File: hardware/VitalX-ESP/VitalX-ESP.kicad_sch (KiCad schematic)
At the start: 56 parts, among them J1 EGC Probe, J2 GSR Probe, J3 UART, J4 JTAG, J5 Power terminal, Q1 BSS138, SW2 Reset, U1 AD8232ACPZ-R7, U3 ADP160AUJZ-1.8-R7, U4 ADPD144RI-ACEZ-RL, U5 AMS1117-3.3, U6 MCP601-xOT, U7 ESP32-S2-WROOM

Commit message: [nightly] Change naming convertion.
+3.3V -> +3V3.
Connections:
- net +3.3V is gone; now on net +3V3: C5.2, R13.2, R15.2, R3.2, R4.2, U1.15 (FR), U1.17 (VS+)
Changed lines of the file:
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@@
     (rev "Sample A")
   )
-  (junction (at 135.255 224.155) (diameter 0) (color 0 0 0 0)
-  )
   (junction (at 99.695 66.675) (diameter 0) (color 0 0 0 0)
   )
@@
   (junction (at 74.295 203.835) (diameter 0) (color 0 0 0 0)
   )
+  (junction (at 135.255 224.155) (diameter 0) (color 0 0 0 0)
+  )
   (junction (at 88.265 227.965) (diameter 0) (color 0 0 0 0)
   )
@@
     )
   )
+  (symbol (lib_id "power:+3V3") (at 184.15 103.505 0) (unit 1)
+    (in_bom yes) (on_board yes) (dnp no) (fields_autoplaced)
+    (property "Reference" "#PWR09" (at 184.15 107.315 0)
+      (effects (font (size 1.27 1.27)) hide)
+    )
+    (property "Value" "+3V3" (at 184.15 99.06 0)
+      (effects (font (size 1.27 1.27)))
+    )
+    (property "Footprint" "" (at 184.15 103.505 0)
+      (effects (font (size 1.27 1.27)) hide)
+    )
+    (property "Datasheet" "" (at 184.15 103.505 0)
+      (effects (font (size 1.27 1.27)) hide)
+    )
+    (pin "1")
+    (instances
+      (project "VitalX-ESP"
+        (path "/c6ad7dc7-b487-4ed9-a043-5d3a4b3b13ea"
+          (reference "#PWR09") (unit 1)
+        )
+      )
+    )
+  )
   (symbol (lib_id "Switch:SW_Push") (at 88.9 109.855 0) (unit 1)
     (in_bom yes) (on_board yes) (dnp no) (fields_autoplaced)
@@
     )
   )
+  (symbol (lib_id "power:+3V3") (at 74.295 201.295 0) (unit 1)
+    (in_bom yes) (on_board yes) (dnp no) (fields_autoplaced)
+    (property "Reference" "#PWR06" (at 74.295 205.105 0)
+      (effects (font (size 1.27 1.27)) hide)
+    )
+    (property "Value" "+3V3" (at 74.295 196.85 0)
+      (effects (font (size 1.27 1.27)))
+    )
+    (property "Footprint" "" (at 74.295 201.295 0)
+      (effects (font (size 1.27 1.27)) hide)
+    )
+    (property "Datasheet" "" (at 74.295 201.295 0)
+      (effects (font (size 1.27 1.27)) hide)
+    )
+    (pin "1")
+    (instances
+      (project "VitalX-ESP"
+        (path "/c6ad7dc7-b487-4ed9-a043-5d3a4b3b13ea"
+          (reference "#PWR06") (unit 1)
+        )
+      )
+    )
+  )
   (symbol (lib_id "Device:R") (at 143.51 213.995 90) (unit 1)
     (in_bom yes) (on_board yes) (dnp no)
@@
     )
   )
+  (symbol (lib_id "power:+3V3") (at 135.255 224.155 0) (unit 1)
+    (in_bom yes) (on_board yes) (dnp no) (fields_autoplaced)
+    (property "Reference" "#PWR07" (at 135.255 227.965 0)
+      (effects (font (size 1.27 1.27)) hide)
+    )
+    (property "Value" "+3V3" (at 135.255 219.71 0)
+      (effects (font (size 1.27 1.27)))
+    )
+    (property "Footprint" "" (at 135.255 224.155 0)
+      (effects (font (size 1.27 1.27)) hide)
+    )
+    (property "Datasheet" "" (at 135.255 224.155 0)
+      (effects (font (size 1.27 1.27)) hide)
+    )
+    (pin "1")
+    (instances
+      (project "VitalX-ESP"
+        (path "/c6ad7dc7-b487-4ed9-a043-5d3a4b3b13ea"
+          (reference "#PWR07") (unit 1)
+        )
+      )
+    )
+  )
   (symbol (lib_id "Device:C_Small") (at 114.935 206.375 90) (unit 1)
     (in_bom yes) (on_board yes) (dnp no)
@@
     )
   )
+  (symbol (lib_id "power:+3V3") (at 107.315 183.515 0) (unit 1)
+    (in_bom yes) (on_board yes) (dnp no) (fields_autoplaced)
+    (property "Reference" "#PWR052" (at 107.315 187.325 0)
+      (effects (font (size 1.27 1.27)) hide)
+    )
+    (property "Value" "+3V3" (at 107.315 179.07 0)
+      (effects (font (size 1.27 1.27)))
+    )
+    (property "Footprint" "" (at 107.315 183.515 0)
+      (effects (font (size 1.27 1.27)) hide)
+    )
+    (property "Datasheet" "" (at 107.315 183.515 0)
+      (effects (font (size 1.27 1.27)) hide)
+    )
+    (pin "1")
+    (instances
+      (project "VitalX-ESP"
+        (path "/c6ad7dc7-b487-4ed9-a043-5d3a4b3b13ea"
+          (reference "#PWR052") (unit 1)
+        )
+      )
+    )
+  )
   (symbol (lib_id "Device:R") (at 81.915 210.185 180) (unit 1)
     (in_bom yes) (on_board yes) (dnp no)
@@
     )
   )
-  (symbol (lib_id "power:+3.3V") (at 184.15 103.505 0) (unit 1)
-    (in_bom yes) (on_board yes) (dnp no)
-    (property "Reference" "#PWR012" (at 184.15 107.315 0)
-      (effects (font (size 1.27 1.27)) hide)
-    )
-    (property "Value" "+3.3V" (at 181.61 99.695 0)
-      (effects (font (size 1.27 1.27)) (justify left))
-    )
-    (property "Footprint" "" (at 184.15 103.505 0)
-      (effects (font (size 1.27 1.27)) hide)
-    )
-    (property "Datasheet" "" (at 184.15 103.505 0)
-      (effects (font (size 1.27 1.27)) hide)
-    )
-    (pin "1")
-    (instances
-      (project "VitalX-ESP"
-        (path "/c6ad7dc7-b487-4ed9-a043-5d3a4b3b13ea"
-          (reference "#PWR012") (unit 1)
-        )
-      )
-    )
-  )
   (symbol (lib_id "power:GND") (at 145.415 233.045 90) (unit 1)
     (in_bom yes) (on_board yes) (dnp no)
@@
     )
   )
-  (symbol (lib_id "power:+3.3V") (at 145.415 230.505 270) (unit 1)
-    (in_bom yes) (on_board yes) (dnp no)
-    (property "Reference" "#PWR04" (at 141.605 230.505 0)
-      (effects (font (size 1.27 1.27)) hide)
-    )
-    (property "Value" "+3.3V" (at 147.955 230.505 90)
-      (effects (font (size 1.27 1.27)) (justify left))
-    )
-    (property "Footprint" "" (at 145.415 230.505 0)
-      (effects (font (size 1.27 1.27)) hide)
-    )
-    (property "Datasheet" "" (at 145.415 230.505 0)
-      (effects (font (size 1.27 1.27)) hide)
-    )
-    (pin "1")
-    (instances
-      (project "VitalX-ESP"
-        (path "/c6ad7dc7-b487-4ed9-a043-5d3a4b3b13ea"
-          (reference "#PWR04") (unit 1)
-        )
-      )
-    )
-  )
   (symbol (lib_id "power:GND") (at 320.04 61.595 0) (unit 1)
     (in_bom yes) (on_board yes) (dnp no) (fields_autoplaced)
@@
     )
   )
+  (symbol (lib_id "power:+3V3") (at 145.415 230.505 270) (unit 1)
+    (in_bom yes) (on_board yes) (dnp no) (fields_autoplaced)
+    (property "Reference" "#PWR04" (at 141.605 230.505 0)
+      (effects (font (size 1.27 1.27)) hide)
+    )
+    (property "Value" "+3V3" (at 148.59 230.505 90)
+      (effects (font (size 1.27 1.27)) (justify left))
+    )
+    (property "Footprint" "" (at 145.415 230.505 0)
+      (effects (font (size 1.27 1.27)) hide)
+    )
+    (property "Datasheet" "" (at 145.415 230.505 0)
+      (effects (font (size 1.27 1.27)) hide)
+    )
+    (pin "1")
+    (instances
+      (project "VitalX-ESP"
+        (path "/c6ad7dc7-b487-4ed9-a043-5d3a4b3b13ea"
+          (reference "#PWR04") (unit 1)
+        )
+      )
+    )
+  )
   (symbol (lib_id "Device:R") (at 92.075 250.825 180) (unit 1)
     (in_bom yes) (on_board yes) (dnp no)
@@
     )
   )
-  (symbol (lib_id "power:+3.3V") (at 135.255 224.155 0) (unit 1)
-    (in_bom yes) (on_board yes) (dnp no)
-    (property "Reference" "#PWR07" (at 135.255 227.965 0)
-      (effects (font (size 1.27 1.27)) hide)
-    )
-    (property "Value" "+3.3V" (at 132.08 220.345 0)
-      (effects (font (size 1.27 1.27)) (justify left))
-    )
-    (property "Footprint" "" (at 135.255 224.155 0)
-      (effects (font (size 1.27 1.27)) hide)
-    )
-    (property "Datasheet" "" (at 135.255 224.155 0)
-      (effects (font (size 1.27 1.27)) hide)
-    )
-    (pin "1")
-    (instances
-      (project "VitalX-ESP"
-        (path "/c6ad7dc7-b487-4ed9-a043-5d3a4b3b13ea"
-          (reference "#PWR07") (unit 1)
-        )
-      )
-    )
-  )
   (symbol (lib_id "AD8232ACPZ:AD8232ACPZ-R7") (at 95.885 213.995 0) (unit 1)
     (in_bom yes) (on_board yes) (dnp no)
@@
     )
   )
-  (symbol (lib_id "power:+3.3V") (at 74.295 201.295 0) (unit 1)
-    (in_bom yes) (on_board yes) (dnp no)
-    (property "Reference" "#PWR06" (at 74.295 205.105 0)
-      (effects (font (size 1.27 1.27)) hide)
-    )
-    (property "Value" "+3.3V" (at 74.295 197.485 0)
-      (effects (font (size 1.27 1.27)))
-    )
-    (property "Footprint" "" (at 74.295 201.295 0)
-      (effects (font (size 1.27 1.27)) hide)
-    )
-    (property "Datasheet" "" (at 74.295 201.295 0)
-      (effects (font (size 1.27 1.27)) hide)
-    )
-    (pin "1")
-    (instances
-      (project "VitalX-ESP"
-        (path "/c6ad7dc7-b487-4ed9-a043-5d3a4b3b13ea"
-          (reference "#PWR06") (unit 1)
-        )
-      )
-    )
-  )
   (symbol (lib_id "power:GND") (at 107.315 188.595 0) (unit 1)
     (in_bom yes) (on_board yes) (dnp no) (fields_autoplaced)
@@
         )
       )
-    )
-  )
-  (symbol (lib_id "power:+3.3V") (at 107.315 183.515 0) (unit 1)
-    (in_bom yes) (on_board yes) (dnp no)
-    (property "Reference" "#PWR09" (at 107.315 187.325 0)
-      (effects (font (size 1.27 1.27)) hide)
-    )
-    (property "Value" "+3.3V" (at 107.315 179.705 0)
-      (effects (font (size 1.27 1.27)))
-    )
-    (property "Footprint" "" (at 107.315 183.515 0)
-      (effects (font (size 1.27 1.27)) hide)
-    )
-    (property "Datasheet" "" (at 107.315 183.515 0)
-      (effects (font (size 1.27 1.27)) hide)
-    )
-    (pin "1")
-    (instances
-      (project "VitalX-ESP"
-        (path "/c6ad7dc7-b487-4ed9-a043-5d3a4b3b13ea"
-          (reference "#PWR09") (unit 1)
-        )
-      )

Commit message: [nightly] Change ECG Probe footprint.
Changes in accordance with reference design.
- https://www.snapeda.com/parts/SJ2-3593D-SMT-TR/CUI%20Devices/view-part/?ref=mouser
- https://easyeda.com/editor#project_id=8294b8a1d6874413ae900972098163d6
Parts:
- removed J1: EGC Probe, Connector_Audio:Jack_3.5mm_KoreanHropartsElec_PJ-320D-4A_Horizontal, symbol Connector_Audio:AudioJack4
- added J1: ECG Probe, AUDIO_SJ2-3593D-SMT-TR:SJ2-3593D-SMT-TR, symbol Connector_Audio:AudioJack3
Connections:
- net LA: now also J1.R
- net RA: now also J1.T
- net RL: now also J1.S
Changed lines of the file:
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@@
     (stroke (width 0) (type default))
   )
-  (wire (pts (xy 45.085 194.31) (xy 53.975 194.31))
-    (stroke (width 0) (type default))
-  )
   (wire (pts (xy 353.695 194.31) (xy 353.695 198.12))
     (stroke (width 0) (type default))
@@
     (effects (font (size 1.27 1.27)) (justify left bottom))
   )
-  (label "RA" (at 53.975 196.85 180) (fields_autoplaced)
+  (label "RA" (at 53.975 201.93 180) (fields_autoplaced)
     (effects (font (size 1.27 1.27)) (justify right bottom))
   )
@@
     (effects (font (size 1.27 1.27)) (justify left bottom))
   )
-  (label "RL" (at 53.975 201.93 180) (fields_autoplaced)
+  (label "RL" (at 53.975 196.85 180) (fields_autoplaced)
     (effects (font (size 1.27 1.27)) (justify right bottom))
   )
@@
     )
   )
+  (symbol (lib_id "Connector_Audio:AudioJack3") (at 40.005 199.39 0) (unit 1)
+    (in_bom yes) (on_board yes) (dnp no)
+    (property "Reference" "J1" (at 39.37 191.135 0)
+      (effects (font (size 1.27 1.27)))
+    )
+    (property "Value" "ECG Probe" (at 39.37 193.675 0)
+      (effects (font (size 1.27 1.27)))
+    )
+    (property "Footprint" "AUDIO_SJ2-3593D-SMT-TR:SJ2-3593D-SMT-TR" (at 40.005 199.39 0)
+      (effects (font (size 1.27 1.27)) hide)
+    )
+    (property "Datasheet" "~" (at 40.005 199.39 0)
+      (effects (font (size 1.27 1.27)) hide)
+    )
+    (pin "S")
+    (pin "T")
+    (pin "R")
+    (instances
+      (project "VitalX-ESP"
+        (path "/c6ad7dc7-b487-4ed9-a043-5d3a4b3b13ea"
+          (reference "J1") (unit 1)
+        )
+      )
+    )
+  )
   (symbol (lib_id "power:+5V") (at 384.81 32.385 0) (unit 1)
     (in_bom yes) (on_board yes) (dnp no) (fields_autoplaced)
@@
     )
   )
-  (symbol (lib_id "Connector_Audio:AudioJack4") (at 40.005 196.85 0) (unit 1)
-    (in_bom yes) (on_board yes) (dnp no)
-    (property "Reference" "J1" (at 38.735 188.595 0)
-      (effects (font (size 1.27 1.27)))
-    )
-    (property "Value" "EGC Probe" (at 38.735 191.135 0)
-      (effects (font (size 1.27 1.27)))
-    )
-    (property "Footprint" "Connector_Audio:Jack_3.5mm_KoreanHropartsElec_PJ-320D-4A_Horizontal" (at 40.005 196.85 0)
-      (effects (font (size 1.27 1.27)) hide)
-    )
-    (property "Datasheet" "~" (at 40.005 196.85 0)
-      (effects (font (size 1.27 1.27)) hide)
-    )
-    (pin "R2")
-    (pin "S")
-    (pin "T")
-    (pin "R1")
-    (instances
-      (project "VitalX-ESP"
-        (path "/c6ad7dc7-b487-4ed9-a043-5d3a4b3b13ea"
-          (reference "J1") (unit 1)
-        )
-      )
-    )
-  )
   (symbol (lib_id "Device:C_Small") (at 117.475 186.055 180) (unit 1)
     (in_bom yes) (on_board yes) (dnp no)
@@
         )
       )
-    )
-  )
-  (symbol (lib_id "power:GND") (at 53.975 194.31 180) (unit 1)
-    (in_bom yes) (on_board yes) (dnp no) (fields_autoplaced)
-    (property "Reference" "#PWR05" (at 53.975 187.96 0)
-      (effects (font (size 1.27 1.27)) hide)
-    )
-    (property "Value" "GND" (at 53.975 189.865 0)
-      (effects (font (size 1.27 1.27)))
-    )
-    (property "Footprint" "" (at 53.975 194.31 0)
-      (effects (font (size 1.27 1.27)) hide)
-    )
-    (property "Datasheet" "" (at 53.975 194.31 0)
-      (effects (font (size 1.27 1.27)) hide)
-    )
-    (pin "1")
-    (instances
-      (project "VitalX-ESP"
-        (path "/c6ad7dc7-b487-4ed9-a043-5d3a4b3b13ea"
-          (reference "#PWR05") (unit 1)
-        )
-      )

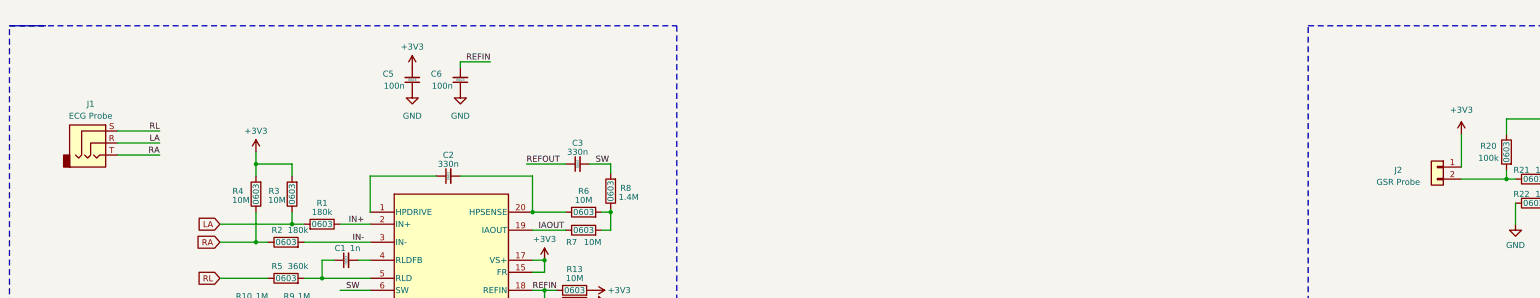
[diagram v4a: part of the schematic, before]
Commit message: [nightly] Adhere to the ECG connector standard.
Mimic Adafruit ECG probe connector design.
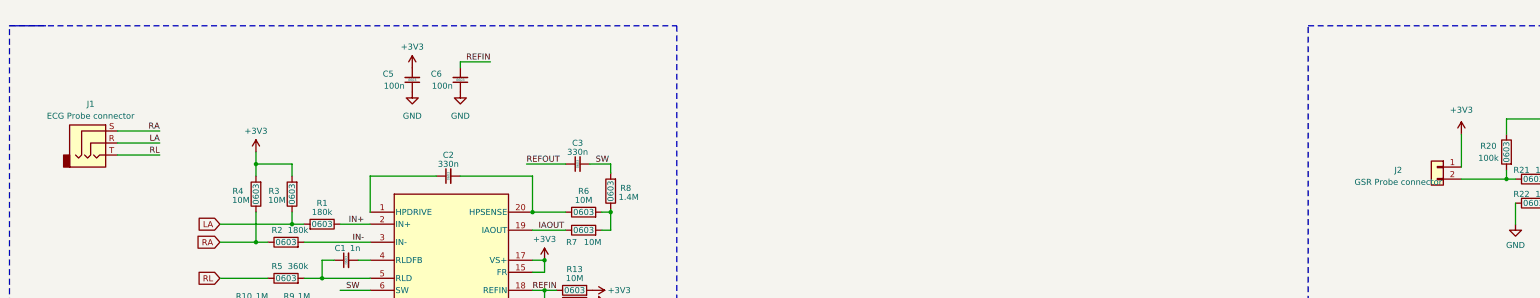
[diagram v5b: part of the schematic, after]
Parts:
- C1, C10, C11, C12, C13, C14, C15, C16, C17, C2, C3, C4, C5, C6, C7, C8, C9: description (none) -> capacitor
- J1: value ECG Probe -> ECG Probe connector; description (none) -> header
- J2: value GSR Probe -> GSR Probe connector; description (none) -> header
- J3, J4, J5: description (none) -> header
- JP1: description (none) -> jumper
- Q1: description (none) -> BSS138; mnf number (none) -> BSS138; mouser mnf num (none) -> 512-BSS138
- R1, R10, R11, R12, R13, R14, R15, R16, R17, R18, R19, R2, R20, R21, R22, R23, R24, R25, R3, R4, R5, R6, R7, R8, R9: description (none) -> resistor
- SW2: description (none) -> button
- U1: description (none) -> AD8232ACPZ-R7; mnf number (none) -> AD8232ACPZ-R7; mouser mnf num (none) -> 584-AD8232ACPZ-R7
- U3: description (none) -> ADP160AUJZ-1.8-R7; mnf number (none) -> ADP160AUJZ-1.8-R7; mouser mnf num (none) -> 584-ADP160AUJZ-1.8R7
- U4: description (none) -> ADPD144RI-ACEZ-RL; mnf number (none) -> ADPD144RI-ACEZ-RL; mouser mnf num (none) -> 584-ADPD144RI-ACEZRL
- U5: description (none) -> AMS1117-3.3; mnf number (none) -> LM1117MPX-3.3/NOPB; mouser mnf num (none) -> 926-LM1117MPX3.3NOPB
- U6: description (none) -> MCP601-xOT; mnf number (none) -> MCP601RT-E/OT; mouser mnf num (none) -> 579-MCP601RT-E/OT
- U7: description (none) -> ESP32-S2-WROOM; mnf number (none) -> ESP32-S2-WROOM-I(M22S2H3200US3Q0); mouser mnf num (none) -> 356-ESP32S2WRMI320US
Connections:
- net RA: now also J1.S; no longer J1.T
- net RL: now also J1.T; no longer J1.S
